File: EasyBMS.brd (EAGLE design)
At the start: 49 x 100 mm, 146 parts, among them Q10 BSS84LT1G, Q11 BSS84LT1G, Q12 BSS84LT1G, Q13 BSS84LT1G, Q2 BSS84LT1G, Q3 BSS84LT1G, Q4 BSS84LT1G, Q5 BSS84LT1G, Q6 BSS84LT1G, Q7 BSS84LT1G, Q8 BSS84LT1G, Q9 BSS84LT1G

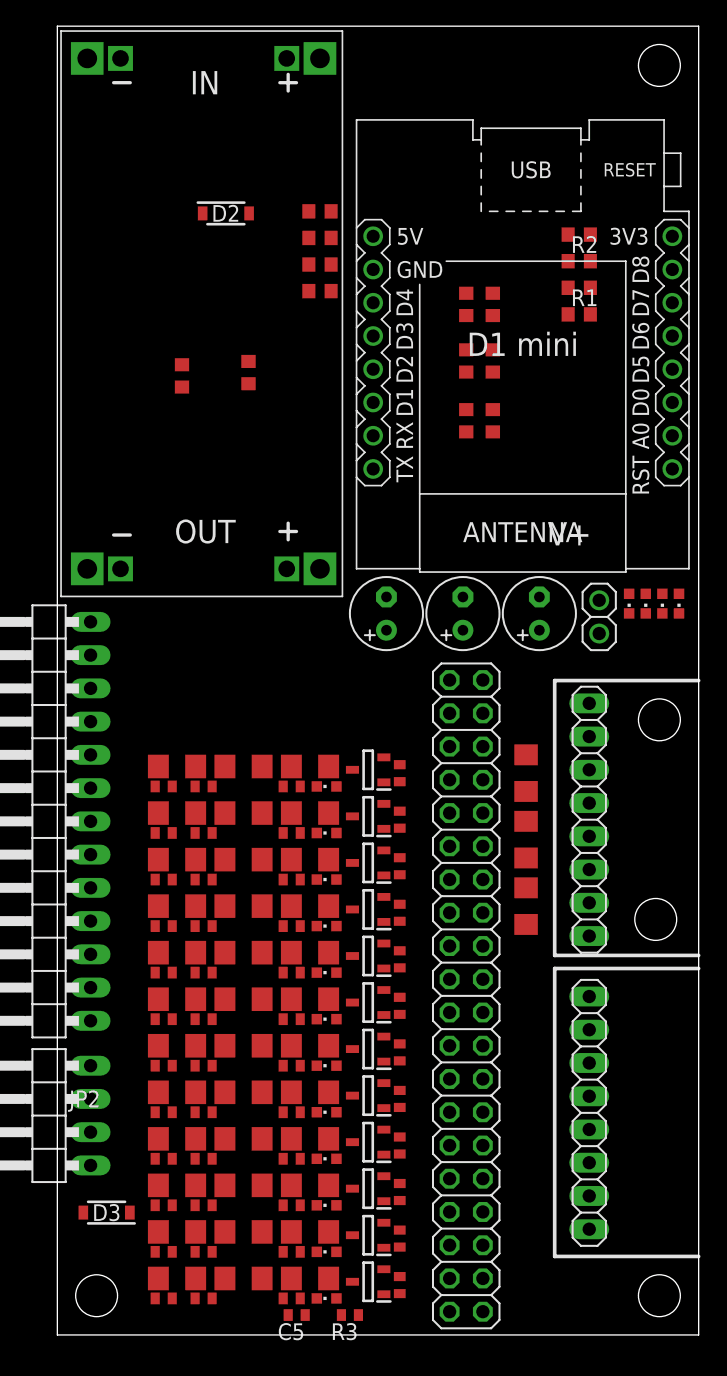
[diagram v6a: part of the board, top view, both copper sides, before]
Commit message: replacing some parts in the layout
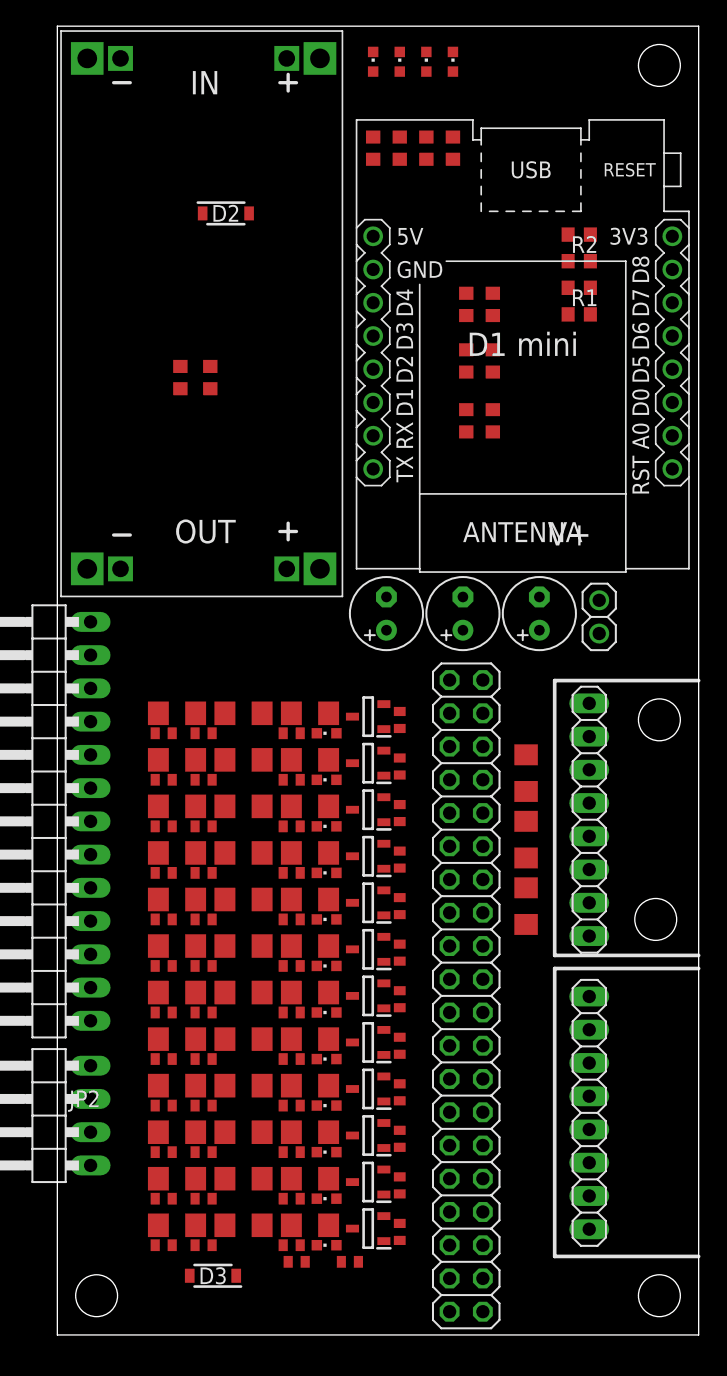
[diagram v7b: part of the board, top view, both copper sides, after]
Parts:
- moved LED1 45.8 mm to (24.1, 97.3), turned to 0 degrees
- moved LED2 45.5 mm to (26.2, 97.3), turned to 0 degrees
- moved LED3 45.2 mm to (28.2, 97.3), turned to 0 degrees
- moved LED4 44.9 mm to (30.2, 97.3), turned to 0 degrees
- moved R53 11.7 mm to (24.1, 90.7), turned to 270 degrees
- moved R56 11.2 mm to (30.2, 90.7), turned to 270 degrees
- moved R54 10.8 mm to (26.2, 90.7), turned to 270 degrees
- moved R55 10.6 mm to (28.2, 90.7), turned to 270 degrees
- moved D3 9.45 mm to (11.9, 4.52)
- moved Q9 4.06 mm to (23.7, 33.0)
- moved R28 4.06 mm to (26.2, 18.5)
- moved R14 4.06 mm to (9.14, 11.9)
- moved R20 4.06 mm to (14.2, 11.9)
- moved R21 4.06 mm to (19.3, 11.9)
- moved C10 4.06 mm to (8.13, 21.1)
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
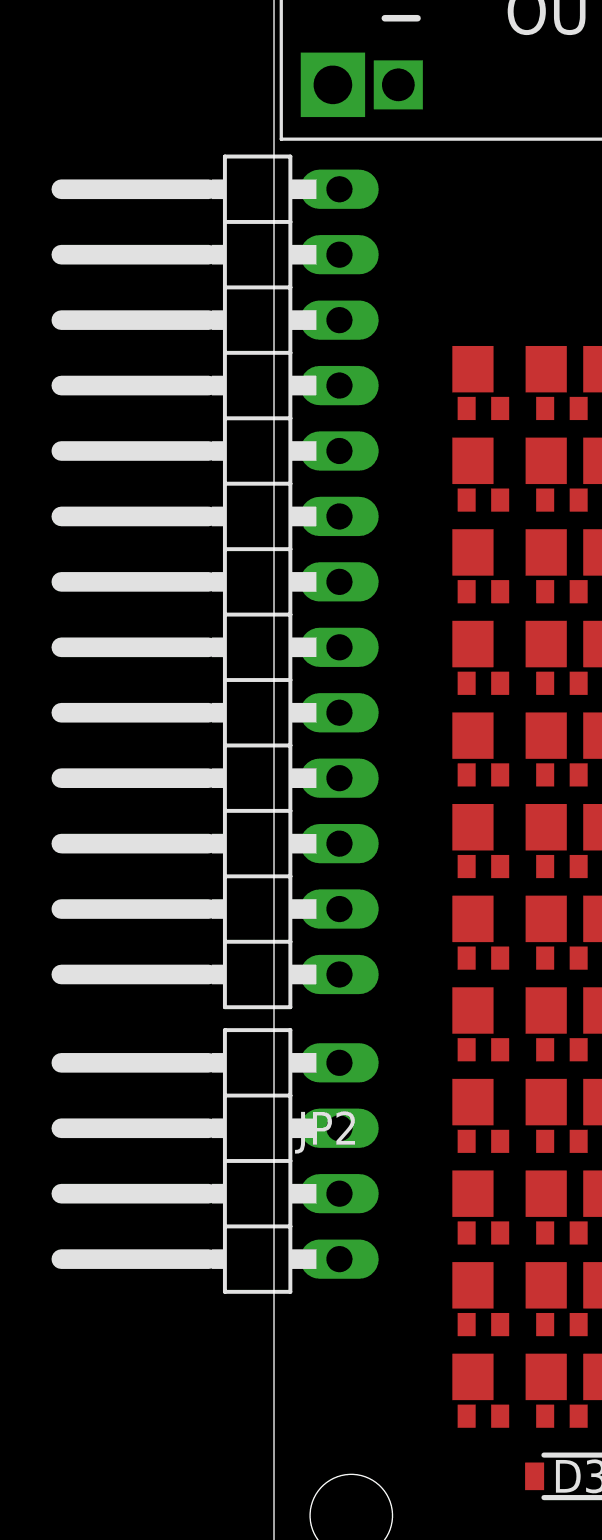
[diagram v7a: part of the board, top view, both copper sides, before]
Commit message: VREF1 set to unused, only VREF2 is used now
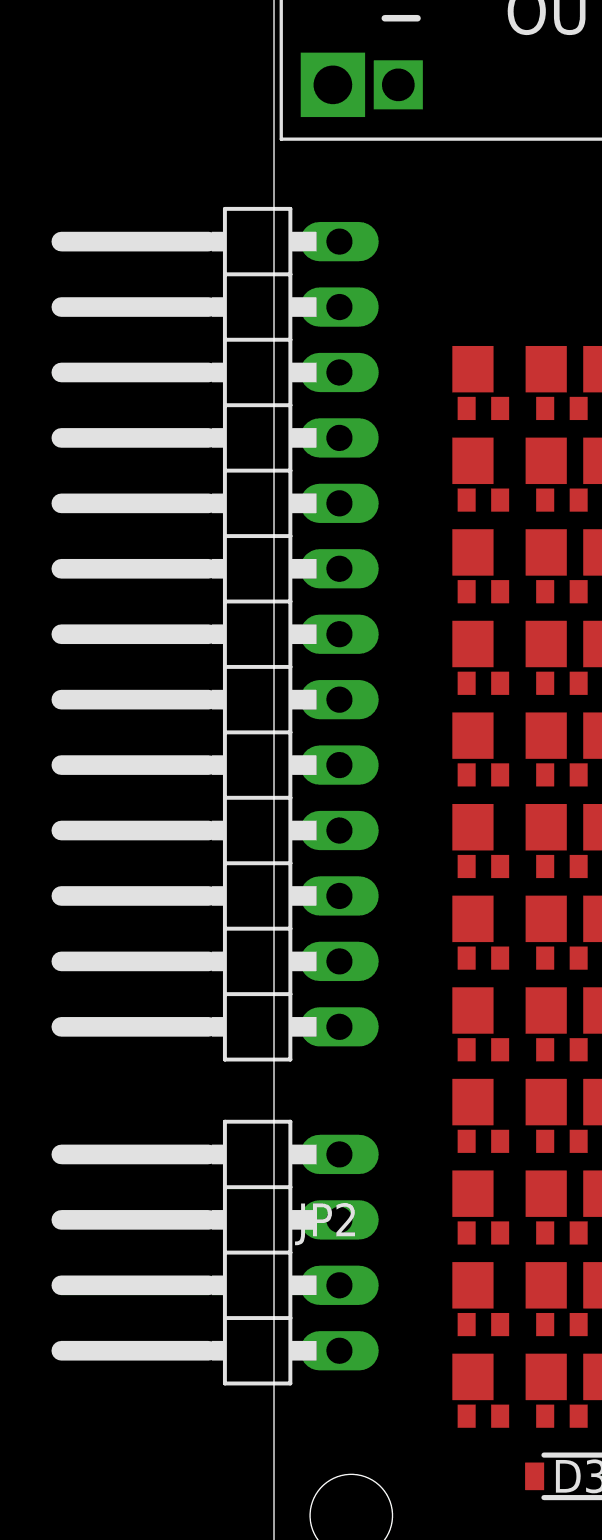
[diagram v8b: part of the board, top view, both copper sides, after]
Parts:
- moved JP2 3.56 mm to (-1.27, 13.2)
- moved JP1 2.03 mm to (-1.27, 37.2)
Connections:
- net VREF1: no longer JP2.3
- net VREF2: now also JP2.3
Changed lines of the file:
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@@
 </element>
 <element name="C1" library="rcl" library_urn="urn:adsk.eagle:library:334" package="E2,5-6" package3d_urn="urn:adsk.eagle:package:23349/1" value="1uF" x="25.146" y="55.118" smashed="yes" rot="R90"/>
-<element name="JP1" library="pinhead" library_urn="urn:adsk.eagle:library:325" package="1X13/90" package3d_urn="urn:adsk.eagle:package:22414/1" value="" x="-1.27" y="39.243" smashed="yes" rot="R90">
-<attribute name="VALUE" x="2.54" y="57.658" size="1.27" layer="27" rot="R180"/>
+<element name="JP1" library="pinhead" library_urn="urn:adsk.eagle:library:325" package="1X13/90" package3d_urn="urn:adsk.eagle:package:22414/1" value="" x="-1.27" y="37.211" smashed="yes" rot="R90">
+<attribute name="VALUE" x="2.54" y="55.626" size="1.27" layer="27" rot="R180"/>
 </element>
 <element name="R15" library="rcl" library_urn="urn:adsk.eagle:library:334" package="R0603" package3d_urn="urn:adsk.eagle:package:23555/2" value="510k" x="33.274" y="78.74" smashed="yes" rot="R270"/>
 <element name="R16" library="rcl" library_urn="urn:adsk.eagle:library:334" package="R0603" package3d_urn="urn:adsk.eagle:package:23555/2" value="27K" x="31.242" y="78.74" smashed="yes" rot="R90"/>
-<element name="JP2" library="pinhead" library_urn="urn:adsk.eagle:library:325" package="1X04/90" package3d_urn="urn:adsk.eagle:package:22404/1" value="" x="-1.27" y="16.764" smashed="yes" rot="R90">
-<attribute name="NAME" x="3.302" y="18.669" size="1.27" layer="25" ratio="10" rot="R180"/>
-<attribute name="VALUE" x="3.175" y="23.749" size="1.27" layer="27" rot="R180"/>
+<element name="JP2" library="pinhead" library_urn="urn:adsk.eagle:library:325" package="1X04/90" package3d_urn="urn:adsk.eagle:package:22404/1" value="" x="-1.27" y="13.208" smashed="yes" rot="R90">
+<attribute name="NAME" x="3.302" y="15.113" size="1.27" layer="25" ratio="10" rot="R180"/>
+<attribute name="VALUE" x="3.175" y="20.193" size="1.27" layer="27" rot="R180"/>
 </element>
 <element name="LED4" library="led" library_urn="urn:adsk.eagle:library:259" package="CHIPLED_0603" package3d_urn="urn:adsk.eagle:package:15822/1" value="KT-0603R" x="30.226" y="97.282" smashed="yes"/>
@@
 <signal name="VREF1">
 <contactref element="C1" pad="+"/>
-<contactref element="JP2" pad="3"/>
 <contactref element="JP5" pad="12"/>
 <contactref element="C18" pad="1"/>
+<wire x1="32.512" y1="37.338" x2="25.146" y2="53.848" width="0" layer="19" extent="1-1"/>
+<wire x1="35.814" y1="36.446" x2="32.512" y2="37.338" width="0" layer="19" extent="1-1"/>
 </signal>
 <signal name="MOSI">
@@
 <contactref element="JP5" pad="14"/>
 <contactref element="C4" pad="1"/>
+<contactref element="JP2" pad="3"/>
+<wire x1="32.512" y1="34.798" x2="30.988" y2="53.848" width="0" layer="19" extent="1-1"/>
+<wire x1="35.814" y1="34.166" x2="32.512" y2="34.798" width="0" layer="19" extent="1-1"/>
+<wire x1="2.54" y1="14.478" x2="32.512" y2="34.798" width="0" layer="19" extent="1-1"/>
+<wire x1="2.54" y1="9.398" x2="2.54" y2="14.478" width="0" layer="19" extent="1-1"/>
 </signal>
 <signal name="GPIO1">
